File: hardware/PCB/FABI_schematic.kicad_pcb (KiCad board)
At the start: 2 copper layers, 81 x 55 mm, 61 parts, among them J1 AudioJack3_Ground, J10 Conn_01x03_Male, J11 display_connector_91601-304LF, J11_GND1 Conn_01x01_Male, J11_VDD1 Conn_01x01_Male, J11_data1 Conn_01x01_Male, J12 009159005551906, J13 Conn_01x04_Male, J2 AudioJack3_Ground, J3 AudioJack3_Ground, J4 AudioJack3_Ground, J5 AudioJack3_Ground, J6 AudioJack3_Ground, J9 Conn_ARM_SWD_TagConnect_TC2030, Q1 BSS806, U1 RaspberryPi_Pico_W_SecondaryP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, U2 TPD3E001DRLR, U3 TSOP4838, U4 TPD3E001DRLR, U5 MIC5504-3.3YM5, U6 TPD3E001DRLR, U7 TPD3E001DRLR

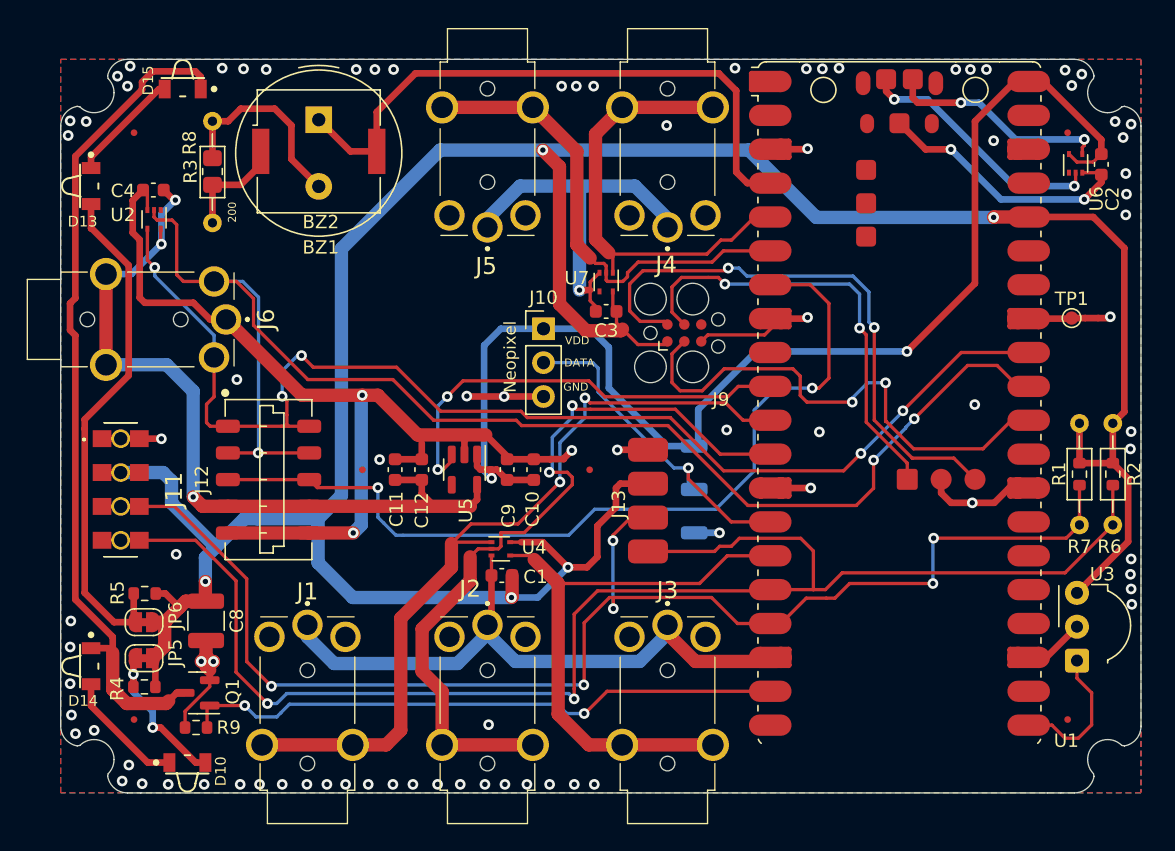
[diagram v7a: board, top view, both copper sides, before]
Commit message: Changed TVS array to a bigger one, cleaned up libraries
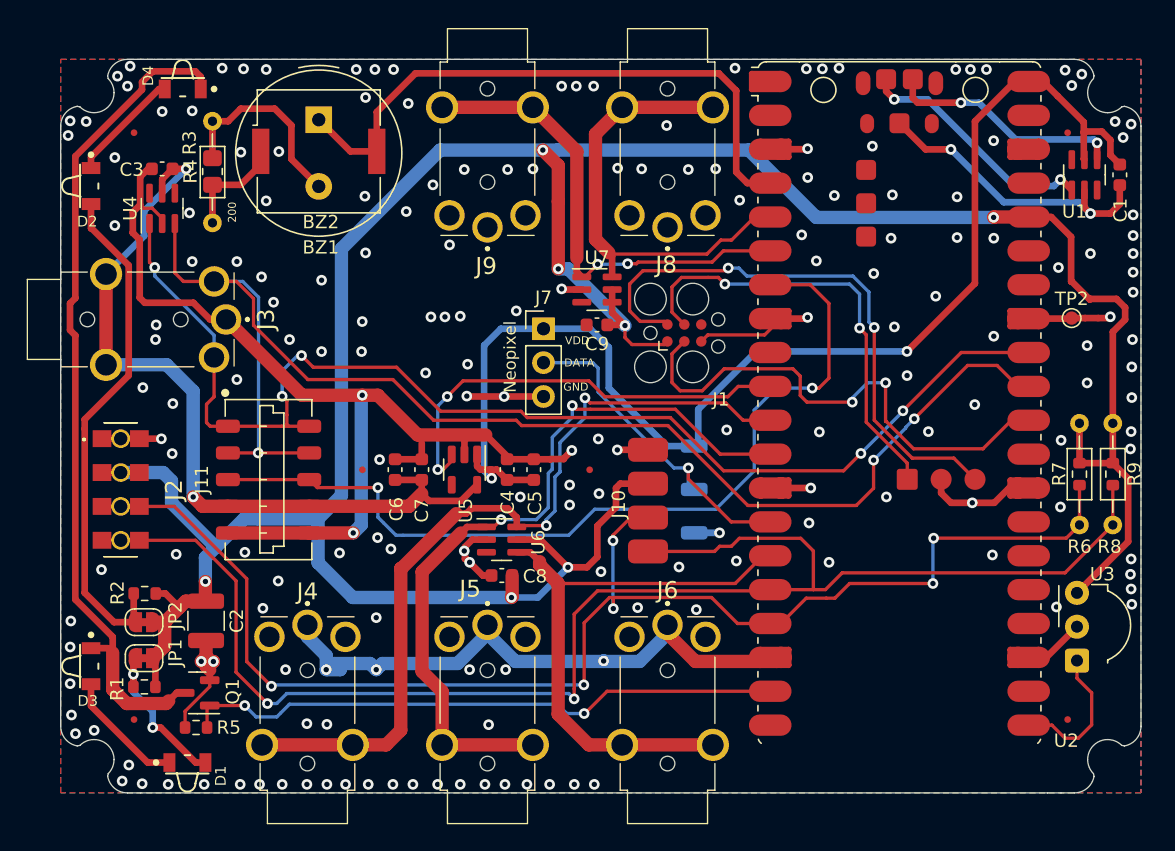
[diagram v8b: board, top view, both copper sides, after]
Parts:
- removed the U2 at (94.2, 95.8)
- added U1: D5V0F4U6SO, Package_SO:SC-74-6_1.5x2.9mm_P0.95mm, F.Cu at (164.0, 92.5)
- U4, U6, U7: value TPD3E001DRLR -> D1213A-04SO-7; footprint Package_TO_SOT_SMD:SOT-553 -> Package_SO:SC-74-6_1.5x2.9mm_P0.95mm
- moved U6 51.5 mm to (120.3, 119.8), turned to 0 degrees
- moved U4 36.0 mm to (94.8, 95.0), turned to 90 degrees
- moved C3 1.72 mm to (94.8, 92.0)
- moved C1 1.59 mm to (166.7, 92.5)
- moved C9 1.22 mm to (127.5, 103.8)
- moved U7 0.89 mm to (127.5, 101.1), turned to 0 degrees
- renumbered C2 to C1, C8 to C2, C4 to C3, C9 to C4, C10 to C5, C11 to C6, C12 to C7, C1 to C8, C3 to C9, D10 to D1, D13 to D2, D14 to D3, D15 to D4, FID7 to FID1, FID8 to FID2, FID9 to FID3, FID10 to FID4, FID11 to FID5, FID12 to FID6, J9 to J1, J13 to J10, J12 to J11, J11 to J2, J6 to J3, J1 to J4, J2 to J5, J3 to J6, J10 to J7, J4 to J8, J5 to J9, JP5 to JP1, JP6 to JP2, LOGO5 to LOGO1, LOGO6 to LOGO2, LOGO7 to LOGO3, LOGO8 to LOGO4, R4 to R1, R5 to R2, R8 to R3, R3 to R4, R9 to R5, R7 to R6, R1 to R7, R6 to R8, R2 to R9, TP1 to TP2, U1 to U2
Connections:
- C1 pad 2: Net-(U1-USB_GND) -> Net-(U1-GND)
- U2 pad TP1: Net-(U1-USB_GND) -> Net-(U1-GND)
- U2 pad TP2: Net-(U1-USB_DM) -> Net-(U1-I/O3)
- U2 pad TP3: Net-(U1-USB_DP) -> Net-(U1-I/O1)
- U4 pad 1: /BUTTON1 -> /SCL
- U4 pad 2: /BUTTON2 -> GNDA
- U4 pad 3: GND -> /SDA
- U4 pad 4: /BUTTON3 -> unconnected-(U4-I/O3-Pad4)
- U4 pad 5: VCC -> +3.3VADC
- U6 pad 1: unconnected-(U6-IO1-Pad1) -> /BUTTON2
- U6 pad 2: Net-(U1-USB_DP) -> GND
- U6 pad 3: Net-(U1-USB_GND) -> unconnected-(U6-I/O2-Pad3)
- U6 pad 4: Net-(U1-USB_DM) -> /BUTTON3
- U6 pad 5: VBUS -> VCC
- U7 pad 1: /BUTTON4 -> /BUTTON5
- U7 pad 2: /BUTTON5 -> GND
- U7 pad 3: GND -> unconnected-(U7-I/O2-Pad3)
- U7 pad 4: unconnected-(U7-IO3-Pad4) -> VCC
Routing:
- net GND: track 136.8 -> 111.8 mm, vias 88 -> 191
- net Net-(U1-GND): track 0.00 -> 23.0 mm, vias 0 -> 2
- net Net-(U1-USB_GND): track 20.1 -> 0.00 mm, vias 2 -> 0
- net Net-(U1-USB_DP): track 19.0 -> 0.00 mm, vias 2 -> 0
- net Net-(U1-I/O1): track 0.00 -> 18.3 mm, vias 0 -> 2
- net Net-(U1-I/O3): track 0.00 -> 17.9 mm, vias 0 -> 2
- net Net-(U1-USB_DM): track 16.7 -> 0.00 mm, vias 2 -> 0
- net GNDA: track 72.3 -> 75.1 mm
- net /SDA: track 105.5 -> 103.2 mm
- net /BUTTON2: track 58.8 -> 57.4 mm
- net VBUS: track 94.3 -> 95.7 mm
- net /BUTTON1: track 62.0 -> 63.0 mm
- net +3.3VADC: track 62.1 -> 61.4 mm, vias 3 -> 2
- net VCC: track 224.1 -> 223.6 mm, vias 5 -> 7
- net /BUTTON5: track 36.7 -> 36.8 mm, vias 0 -> 2
